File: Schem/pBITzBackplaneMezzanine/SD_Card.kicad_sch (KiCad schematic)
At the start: 5 parts, among them J4 10067847-001RLF, U4 CD74HC4050M96

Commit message: Added all the manufacturer part numbers to the KiCad schematics and PCB files. This will make it easier to order the parts for the project and ensure that the correct components are used. I also removed some of the old schematics that were no longer needed, such as the BaudClock, ConsolePort, DeviceSelectDecode, GPIOUserSerial, IO Controller, UserPorts, Video, and Z80HomeBrew schematics. These changes will help to streamline the design and make it easier to understand.
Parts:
- J4: MANUFACTURER_PART_NUMBER (none) -> 10067847-001RLF
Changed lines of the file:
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@@
 			)
 		)
-		(property "Datasheet" "~"
+		(property "Datasheet" "C0603C104K5RACTU"
 			(at 60.96 201.93 0)
 			(effects
@@
 			)
 		)
+		(property "MANUFACTURER_PART_NUMBER" "10067847-001RLF"
+			(at 124.46 72.39 0)
+			(effects
+				(font
+					(size 1.27 1.27)
+				)
+				(hide yes)
+			)
+		)
 		(pin "1"
 		)
@@
 			)
 		)
-		(property "Datasheet" "~"
+		(property "Datasheet" "C0603C104K5RACTU"
 			(at 76.2 76.2 0)
 			(effects

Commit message: Updated the 3d images and exported the image
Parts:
- U4: footprint Footprints:SOIC127P600X175-16N -> Package_SO:SOIC-16_3.9x9.9mm_P1.27mm
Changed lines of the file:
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@@
 			)
 		)
-		(property "Footprint" "Footprints:SOIC127P600X175-16N"
+		(property "Footprint" "Package_SO:SOIC-16_3.9x9.9mm_P1.27mm"
 			(at 97.79 157.48 0)
 			(effects
@@
 			)
 		)
-		(property "Footprint" "Footprints:SOIC127P600X175-16N"
+		(property "Footprint" "Package_SO:SOIC-16_3.9x9.9mm_P1.27mm"
 			(at 119.38 219.71 0)
 			(effects
@@
 			)
 		)
-		(property "Footprint" "Footprints:SOIC127P600X175-16N"
+		(property "Footprint" "Package_SO:SOIC-16_3.9x9.9mm_P1.27mm"
 			(at 97.79 123.19 0)
 			(effects
@@
 			)
 		)
-		(property "Footprint" "Footprints:SOIC127P600X175-16N"
+		(property "Footprint" "Package_SO:SOIC-16_3.9x9.9mm_P1.27mm"
 			(at 119.38 191.77 0)
 			(effects
@@
 			)
 		)
-		(property "Footprint" "Footprints:SOIC127P600X175-16N"
+		(property "Footprint" "Package_SO:SOIC-16_3.9x9.9mm_P1.27mm"
 			(at 97.79 139.7 0)
 			(effects
@@
 			)
 		)
-		(property "Footprint" "Footprints:SOIC127P600X175-16N"
+		(property "Footprint" "Package_SO:SOIC-16_3.9x9.9mm_P1.27mm"
 			(at 81.28 201.93 0)
 			(effects
@@
 			)
 		)
-		(property "Footprint" "Footprints:SOIC127P600X175-16N"
+		(property "Footprint" "Package_SO:SOIC-16_3.9x9.9mm_P1.27mm"
 			(at 119.38 205.74 0)
 			(effects

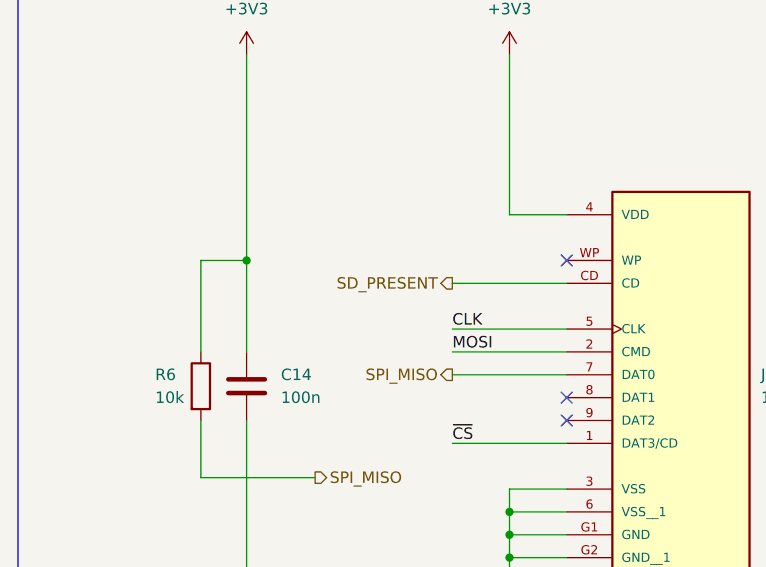
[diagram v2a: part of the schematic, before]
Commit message: Major rework:
- Updated the Mezzanine to remove the slot connector and move it to the main board (facing the back)
-    The removal of the slot allowed for the removal of the FPC connector, which was a
     major source of complexity. The mezzanine now only has the SD card and USB connectors,
     which are much cheaper and easier to work with.
- The mezzanine is now more compact and cheaper to souirce

- The main board sees the addition of the external slot connector (coming from the mezzanine)
- Added power led on the mother board for easier debugging and testing
- Removed the free floating resistors to replace them with resistor packs
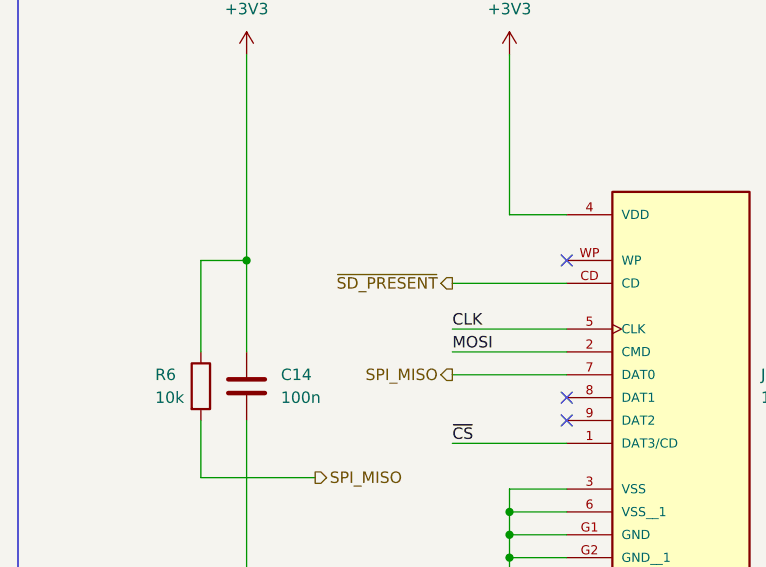
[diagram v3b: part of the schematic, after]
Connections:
- net SD_PRESENT renamed ~{SD_PRESENT}
